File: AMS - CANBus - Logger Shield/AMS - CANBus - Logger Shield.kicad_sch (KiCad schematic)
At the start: 17 parts, among them IC1 DS3231SN#, IC4 CD74HC4050ME4, J1 Power, J2 Digital/PWM, J3 Analog, J4 Digital/PWM, J5 Power_And_CAN, J6 GTFH08131YHR, Q1 IRF9Z34NPBF, U5 3568

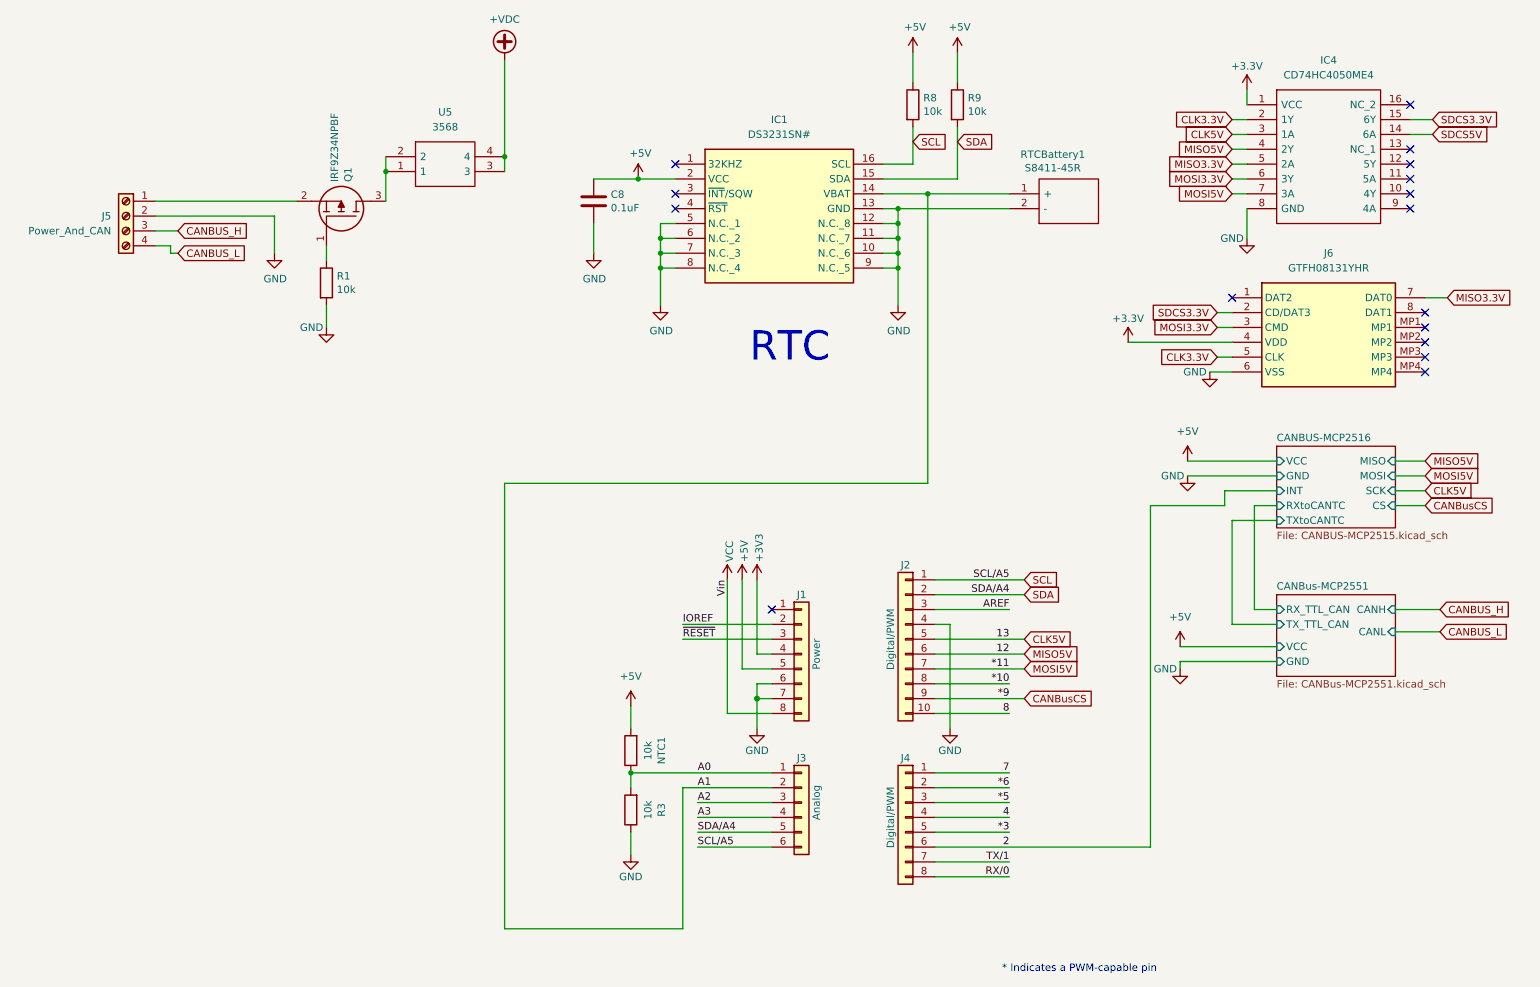
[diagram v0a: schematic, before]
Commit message: Logger Shield fixing the following Fuck ups for 1.0 Rev A * didn't connect the 3.3v lines * didn't connect the 5.5v SD Card Chip Select to the level shifter * didn't connect the VDC to the Vin pin
Did some route optimization with my widdle brain.
Bumped to Rev B since i didn't fix any that was not a complete fuck up or add anything new
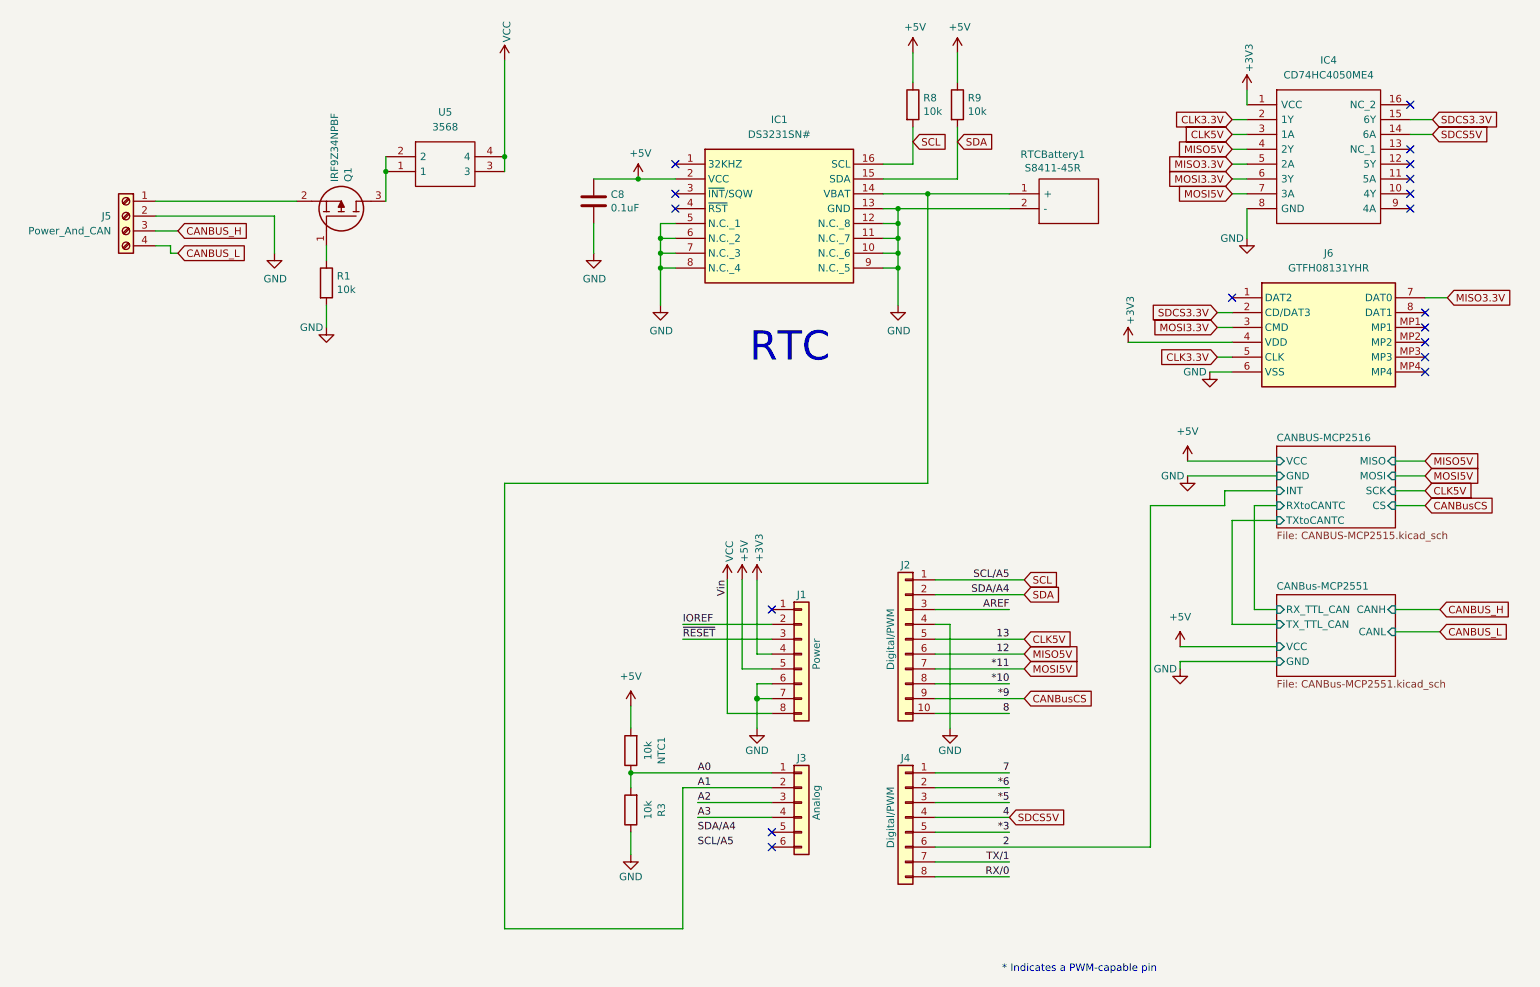
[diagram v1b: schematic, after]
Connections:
- net +3.3V is gone; now on net +3V3: IC4.1 (VCC), J6.4 (VDD)
- net +VDC is gone; now on net VCC: U5.3, U5.4
- net 4 is gone; now on net SDCS5V: J4.4 (Pin_4)
- net SCL: no longer J3.6 (Pin_6)
- net SDA: no longer J3.5 (Pin_5)
- no-connect marks 16 -> 18
